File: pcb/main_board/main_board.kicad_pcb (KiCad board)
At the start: 2 copper layers, 100.3 x 100.3 mm, 36 parts, among them J1 Sensors_Conn, J2 Power_Conn, J3 I2C_Conn, J4 Garage_Conn, J5 Debug_Sensors_Conn, J6 Debug_I2C_Conn, U1 ESP-01, U2 HC_05, U3 AT24CS64-SSHM, U4 AMS1117-3.3, U5 Black_Pill

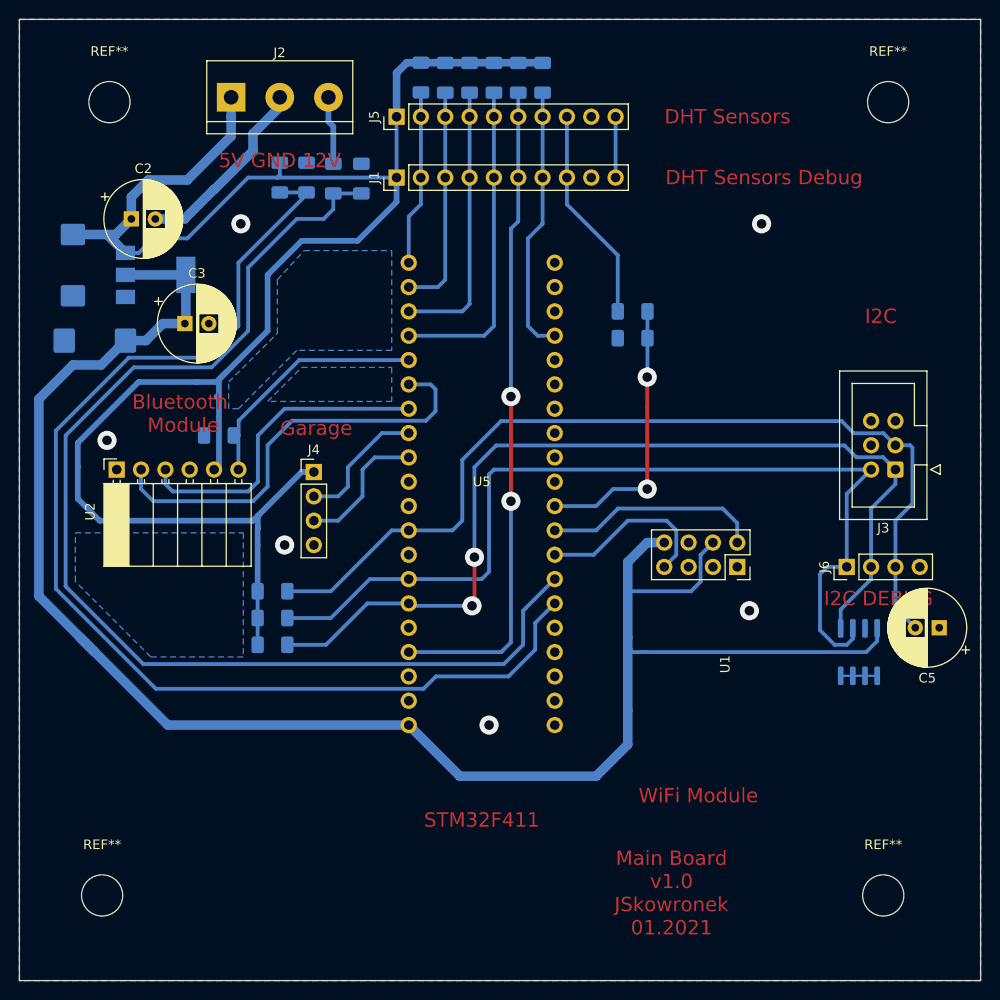
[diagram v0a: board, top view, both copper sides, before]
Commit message: main_baord reworked to one-side board
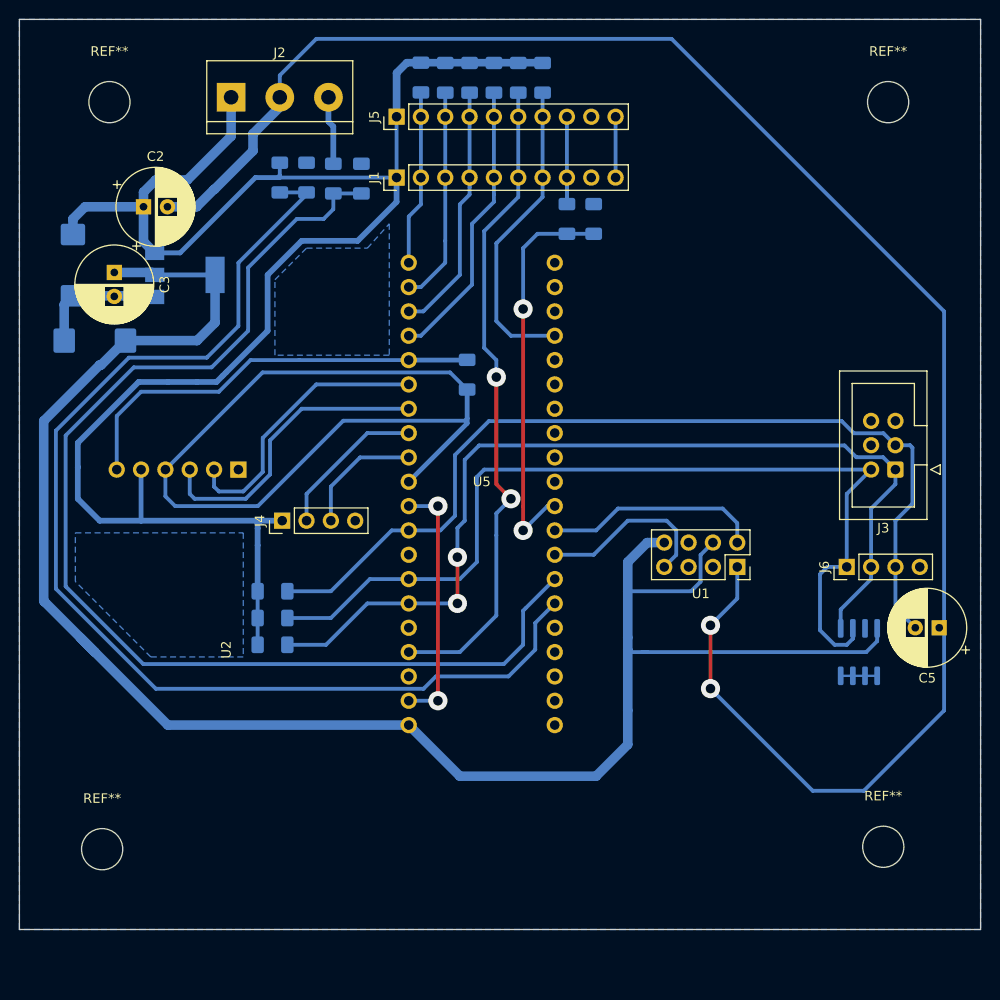
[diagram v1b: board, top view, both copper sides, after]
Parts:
- U2: footprint Connector_PinSocket_2.54mm:PinSocket_1x06_P2.54mm_Horizontal -> project_footprints:HC_05
- moved R4 26.7 mm to (148.3, 100.6), turned to 90 degrees
- moved R14 13.1 mm to (161.5, 84.3), turned to 270 degrees
- moved R16 11.8 mm to (158.8, 84.3), turned to 90 degrees
- moved C3 9.09 mm to (111.5, 89.9), turned to 270 degrees
- moved U2 6.35 mm to (118.1, 110.5), turned to 270 degrees
- moved J4 6.06 mm to (129.0, 115.8), turned to 90 degrees
- moved REF** 5.08 mm to (191.8, 149.9)
- moved REF** 4.83 mm to (110.2, 150.1)
- moved U4 3.05 mm to (118.9, 90.2)
- moved C2 1.80 mm to (114.6, 83.1)
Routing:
- net GND: track 30.1 -> 328.2 mm, vias 6 -> 4
- net BT_KEY: track 25.5 -> 44.6 mm
- net BT_RX_STM_TX: track 45.0 -> 29.0 mm
- net Net-(R14-Pad2): track 28.9 -> 41.8 mm
- net LIGHT_SENSOR: track 22.5 -> 10.7 mm
- net 5V: track 196.1 -> 185.3 mm
- net 3.3V: track 188.1 -> 193.4 mm
- net DHT_SENSOR2: track 28.2 -> 32.6 mm
- net DHT_SENSOR6: track 33.7 -> 29.8 mm
- net DHT_SENSOR5: track 28.7 -> 26.4 mm
- net BT_TX_STM_RX: track 33.6 -> 31.6 mm
- net GARAGE_RX_STM_TX: track 13.8 -> 15.8 mm
- net GARAGE_TX_STM_RX: track 14.3 -> 12.7 mm
- net DHT_SENSOR4: track 23.7 -> 22.6 mm
- net I2C_SCL: track 98.9 -> 98.1 mm
- removed copper zone on F.Cu, net GND
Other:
- board size 100.3 x 100.3 mm -> 100.3 x 95 mm
- board text added: "BLUETOOTH MODULE"
- board text added: "DHT DEBUG"
- board text added: "DHT SENSORS"
- board text added: "GARAGE"
- board text added: "Main board v1.0 JSkowronek 01-2021"
- board text added: "STM MCU"
- board text added: "WIFI MODULE"
- board text removed: "5V GND 12V"
- board text removed: "Bluetooth Module"
- board text removed: "DHT Sensors"
- board text removed: "DHT Sensors Debug"
- board text removed: "Garage"
- board text removed: "Main Board v1.0 JSkowronek 01.2021"
- board text removed: "STM32F411"
- board text removed: "WiFi Module"

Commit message: Main board pcb updated
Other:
- board text added: "5V GND 12V"
